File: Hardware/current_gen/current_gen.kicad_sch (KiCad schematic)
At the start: 26 parts, among them J1 Conn_Coaxial, J2 Conn_Coaxial, J3 Jack-DC, Q1 NPN, Q10 NPN, Q11 NPN, Q12 NPN, Q13 BSP129, Q2 NPN, Q3 NPN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

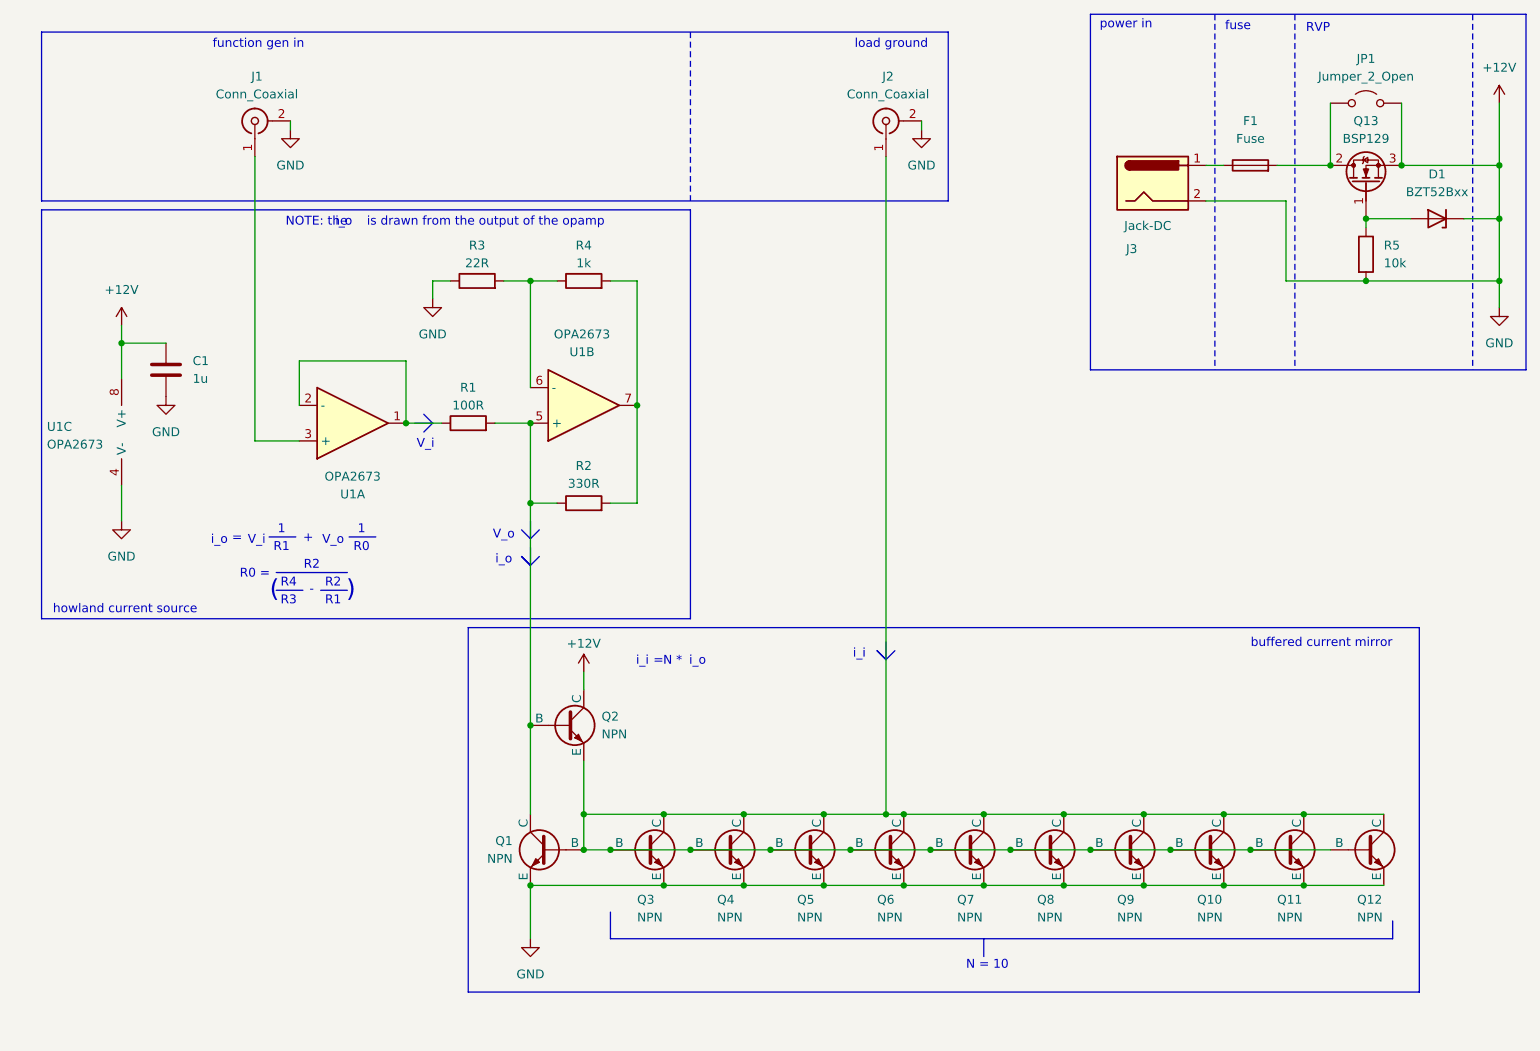
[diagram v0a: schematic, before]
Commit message: added shunt and rpv
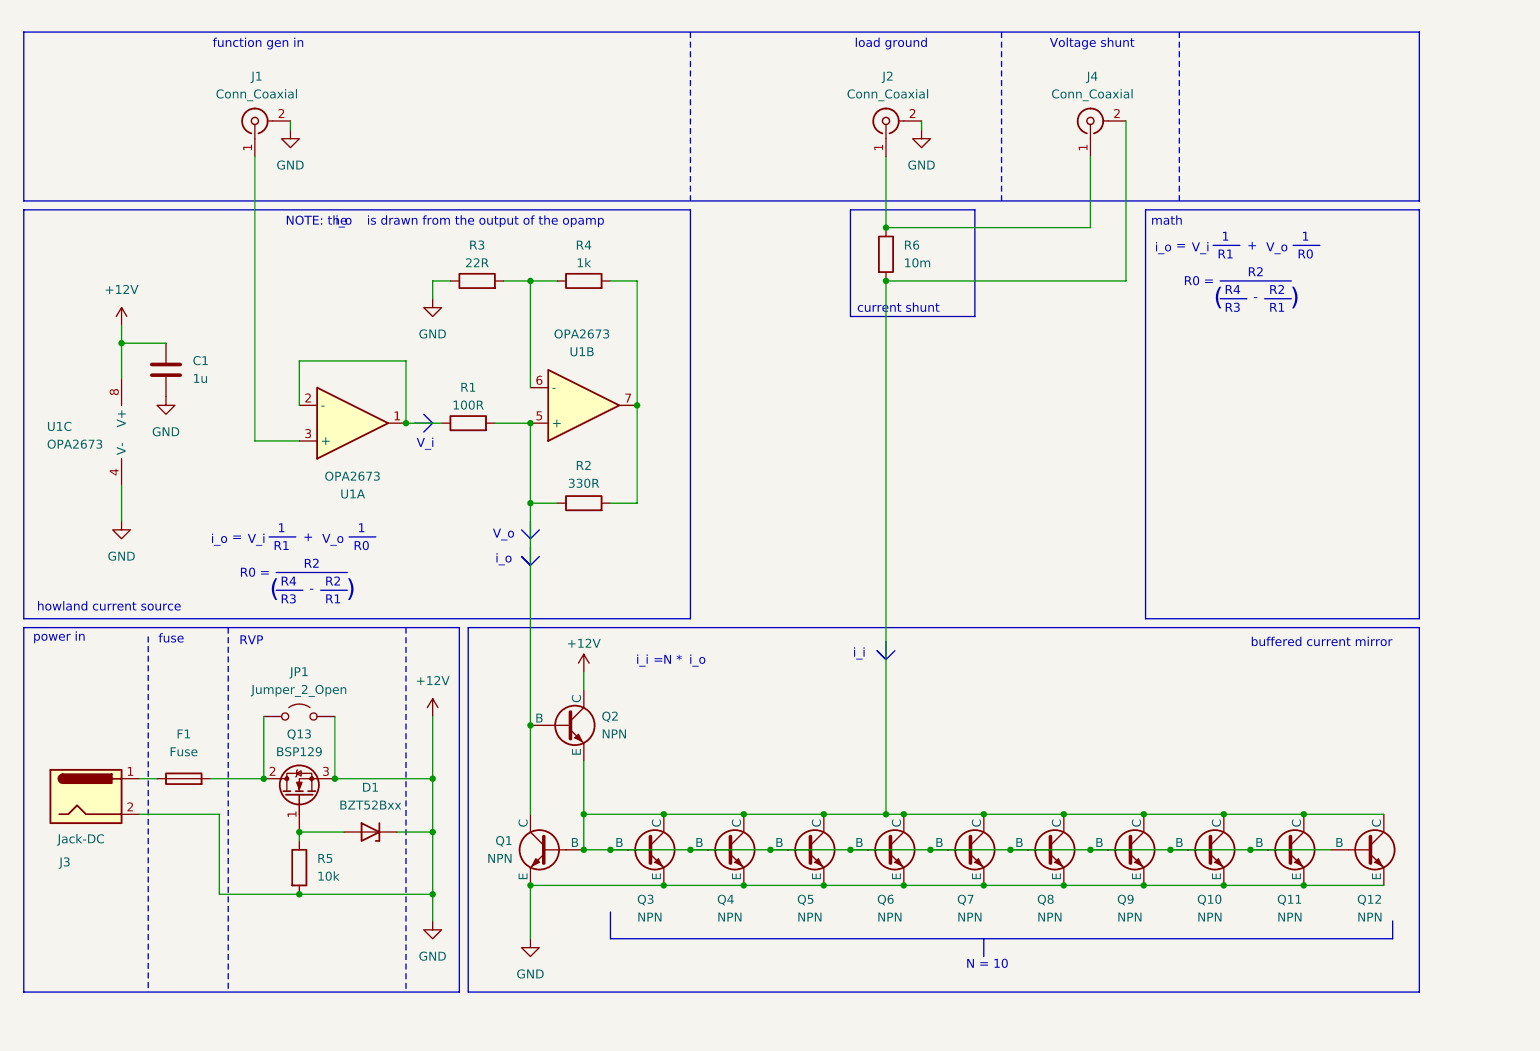
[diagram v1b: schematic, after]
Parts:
- added J4: Conn_Coaxial, symbol Connector:Conn_Coaxial
- added R6: 10m, symbol Device:R
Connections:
- net at Q1.2 (B), Q10.1 (C), Q10.2 (B)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: now also J4.2 (Ext), R6.2; no longer J2.1 (In)
- new net: J2.1 (In), J4.1 (In), R6.1
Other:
- note added: "Voltage shunt"
- note added: "current shunt"
- note added: "math"
- moved on the sheet: D1, F1, J3, JP1, Q13, R5

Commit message: added some docs
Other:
- title: (none) -> constant current function gen
- moved on the sheet: C1, D1, F1, J1, J2, J3, J4, JP1, Q1, Q10, Q11, Q12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
